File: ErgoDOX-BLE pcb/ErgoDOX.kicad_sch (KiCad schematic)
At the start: 102 parts, among them J1 Conn_01x04, J2 Conn_01x02_Female, J3 Conn_01x02_Female, J4 Conn_01x02, J5 Conn_01x02, J6 6PIN, P1 USB_C_Plug_USB2.0, Q1 Q_NPN_BCE, SW0:10 SW0:3, SW0:11 SW0:2, SW0:12 SW0:1, SW0:7 SW0:6, SW0:8 SW0:5, SW0:9 SW0:4, SW1:10 SW1:3, SW1:11 SW1:2, SW1:12 SW1:1, SW1:13 SW1:0, SW1:9 SW1:4, SW2:10 SW2:3, SW2:11 SW2:2, SW2:12 SW2:1, SW2:13 SW2:0, SW2:7 SW2:6, SW2:8 SW2:5, SW2:9 SW2:4, SW3:10 SW3:3, SW3:11 SW3:2, SW3:12 SW3:1, SW3:13 SW3:0, SW3:8 SW3:5, SW3:9 SW3:4, SW4:10 SW4:3, SW4:11 SW4:2, SW4:12 SW4:1, SW4:13 SW4:0, SW4:7 SW4:6, SW4:8 SW4:5, SW4:9 SW4:4, SW5:10 SW5:3, SW5:11 SW5:2, SW5:12 SW5:1, SW5:13 SW5:0, SW5:7 SW5:6, SW5:8 SW5:5, SW5:9 SW5:4, U1 MCP23018, U2 MCP23017_SP

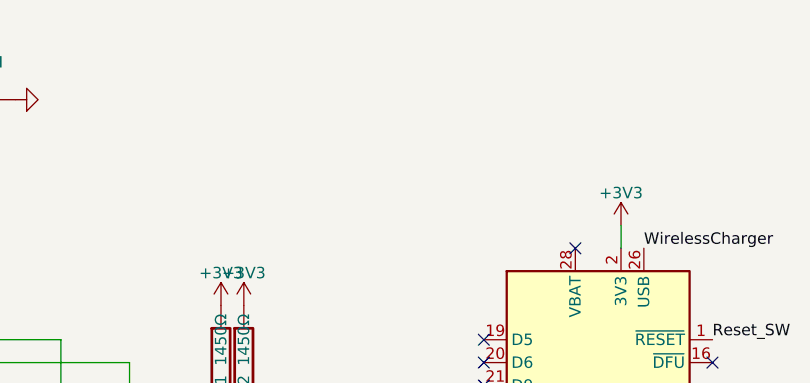
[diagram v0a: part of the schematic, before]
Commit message: Begin playing around with replacing the 23018 with a 23017
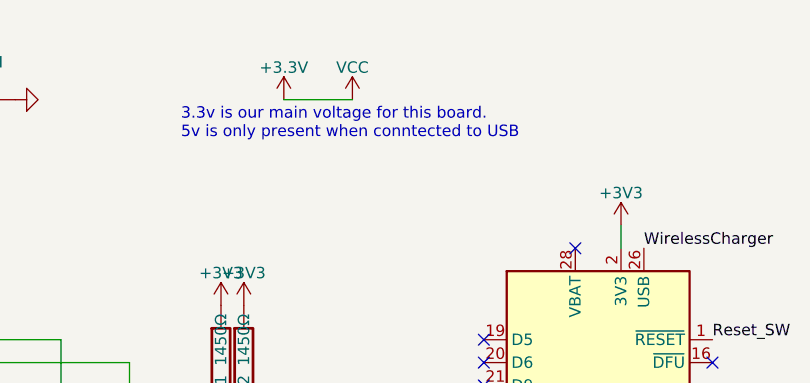
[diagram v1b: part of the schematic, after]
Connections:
- net VCC renamed +3.3V
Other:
- note added: "3.3v is our main voltage for this board. 5v is only present when conntected to USB"
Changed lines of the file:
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@@
     (stroke (width 0) (type default) (color 0 0 0 0))
   )
+  (wire (pts (xy 111.125 21.59) (xy 118.745 21.59))
+    (stroke (width 0) (type default) (color 0 0 0 0))
+  )
   (wire (pts (xy 58.42 196.85) (xy 76.2 196.85))
     (stroke (width 0) (type default) (color 0 0 0 0))
@@
     (effects (font (size 1.27 1.27)) (justify left bottom))
   )
+  (text "3.3v is our main voltage for this board.\n5v is only present when conntected to USB"
+    (at 99.695 26.035 0)
+    (effects (font (size 1.27 1.27)) (justify left bottom))
+  )
   (text "Backside footprint for MCU" (at 153.035 101.6 0)
     (effects (font (size 1.27 1.27)) (justify left bottom))
@@
     (pin "2")
   )
+  (symbol (lib_id "power:+3.3V") (at 111.125 21.59 0) (unit 1)
+    (in_bom yes) (on_board yes) (fields_autoplaced)
+    (property "Reference" "#PWR?" (id 0) (at 111.125 25.4 0)
+      (effects (font (size 1.27 1.27)) hide)
+    )
+    (property "Value" "+3.3V" (id 1) (at 111.125 18.0142 0))
+    (property "Footprint" "" (id 2) (at 111.125 21.59 0)
+      (effects (font (size 1.27 1.27)) hide)
+    )
+    (property "Datasheet" "" (id 3) (at 111.125 21.59 0)
+      (effects (font (size 1.27 1.27)) hide)
+    )
+    (pin "1")
+  )
+  (symbol (lib_id "power:VCC") (at 118.745 21.59 0) (unit 1)
+    (in_bom yes) (on_board yes) (fields_autoplaced)
+    (property "Reference" "#PWR?" (id 0) (at 118.745 25.4 0)
+      (effects (font (size 1.27 1.27)) hide)
+    )
+    (property "Value" "VCC" (id 1) (at 118.745 18.0142 0))
+    (property "Footprint" "" (id 2) (at 118.745 21.59 0)
+      (effects (font (size 1.27 1.27)) hide)
+    )
+    (property "Datasheet" "" (id 3) (at 118.745 21.59 0)
+      (effects (font (size 1.27 1.27)) hide)
+    )
+    (pin "1")
+  )
   (symbol (lib_id "Device:RotaryEncoder_Switch") (at 295.91 140.97 0) (unit 1)
     (in_bom yes) (on_board yes) (fields_autoplaced)
@@
       (reference "#PWR0107") (unit 1) (value "+5V") (footprint "")
     )
+    (path "/a649175b-f354-4397-a3b3-c0bd849b7072"
+      (reference "#PWR?") (unit 1) (value "+3.3V") (footprint "")
+    )
+    (path "/a9287306-e15a-4803-9f71-a2b7ca520be7"
+      (reference "#PWR?") (unit 1) (value "VCC") (footprint "")
+    )
     (path "/dc3e5149-0691-4e48-82aa-18a33c58d220"

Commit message: A lot of footprint work
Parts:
- removed U2: MCP23017_SP, Package_DIP:DIP-28_W7.62mm, symbol Interface_Expansion:MCP23017_SP
- C1: footprint Capacitor_THT:C_Axial_L5.1mm_D3.1mm_P7.50mm_Horizontal -> Capacitor_THT:CP_Radial_Tantal_D5.0mm_P5.00mm
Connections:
- net +3.3V is gone; now on net +3V3: U1.11 (VCC)
- no-connect marks 40 -> 38
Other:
- note added: "TODO: Need to double check the connector on size on this"
- note removed: "3.3v is our main voltage for this board. 5v is only present when conntected to USB"

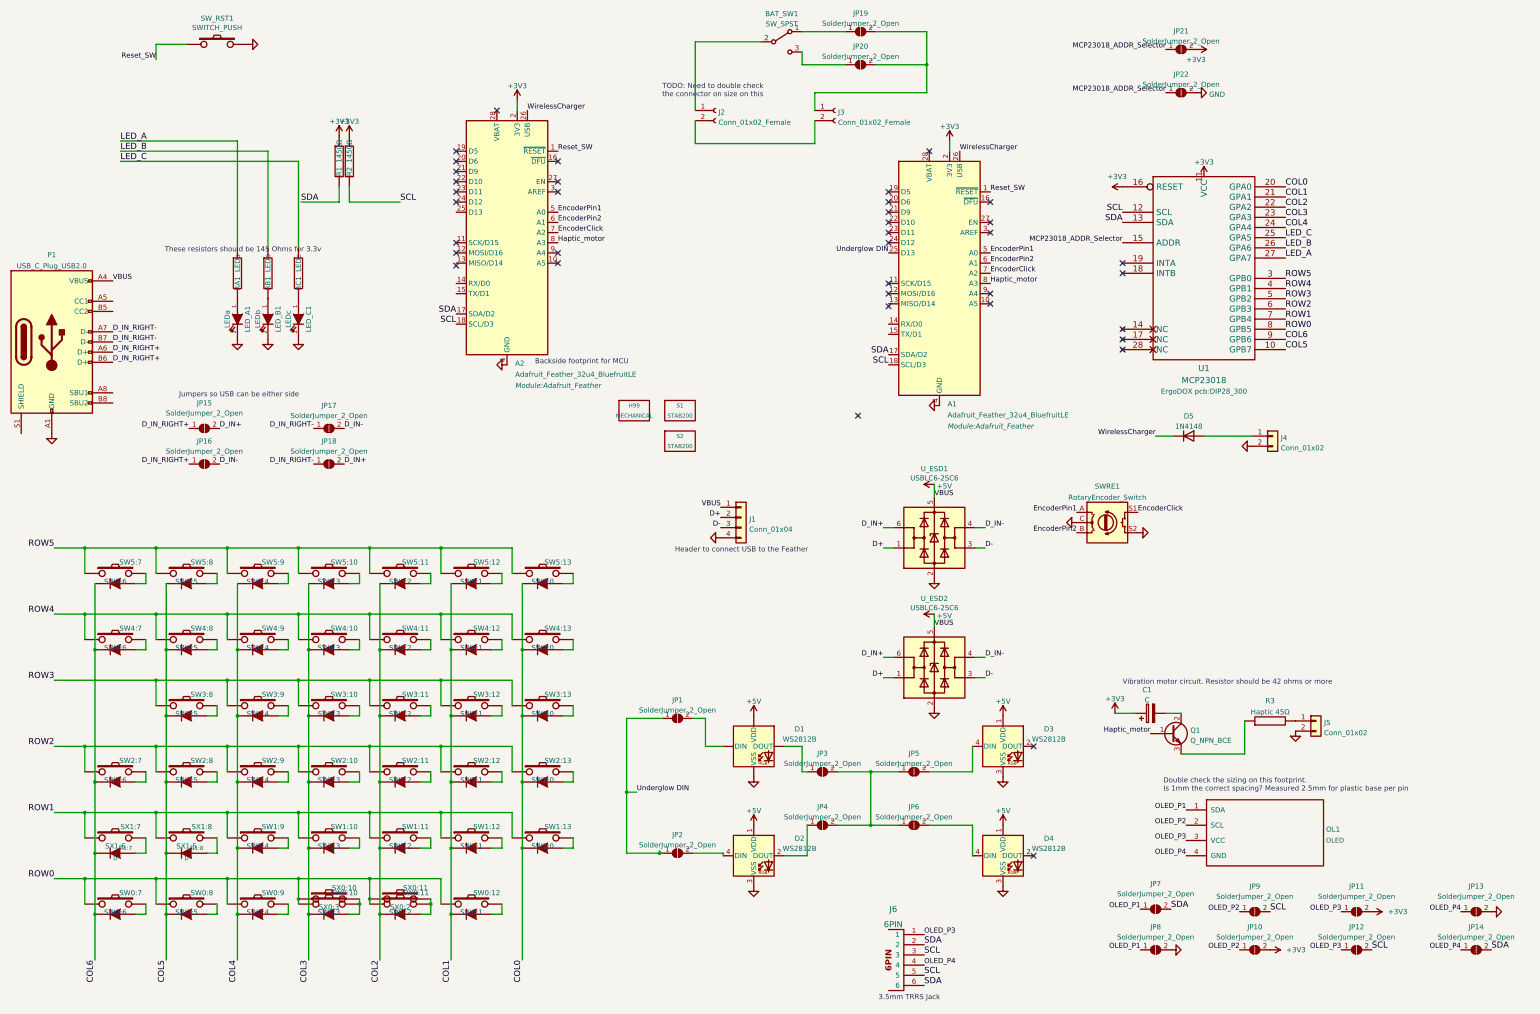
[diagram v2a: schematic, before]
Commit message: Adding a bunch of part numbers and verifying sizing
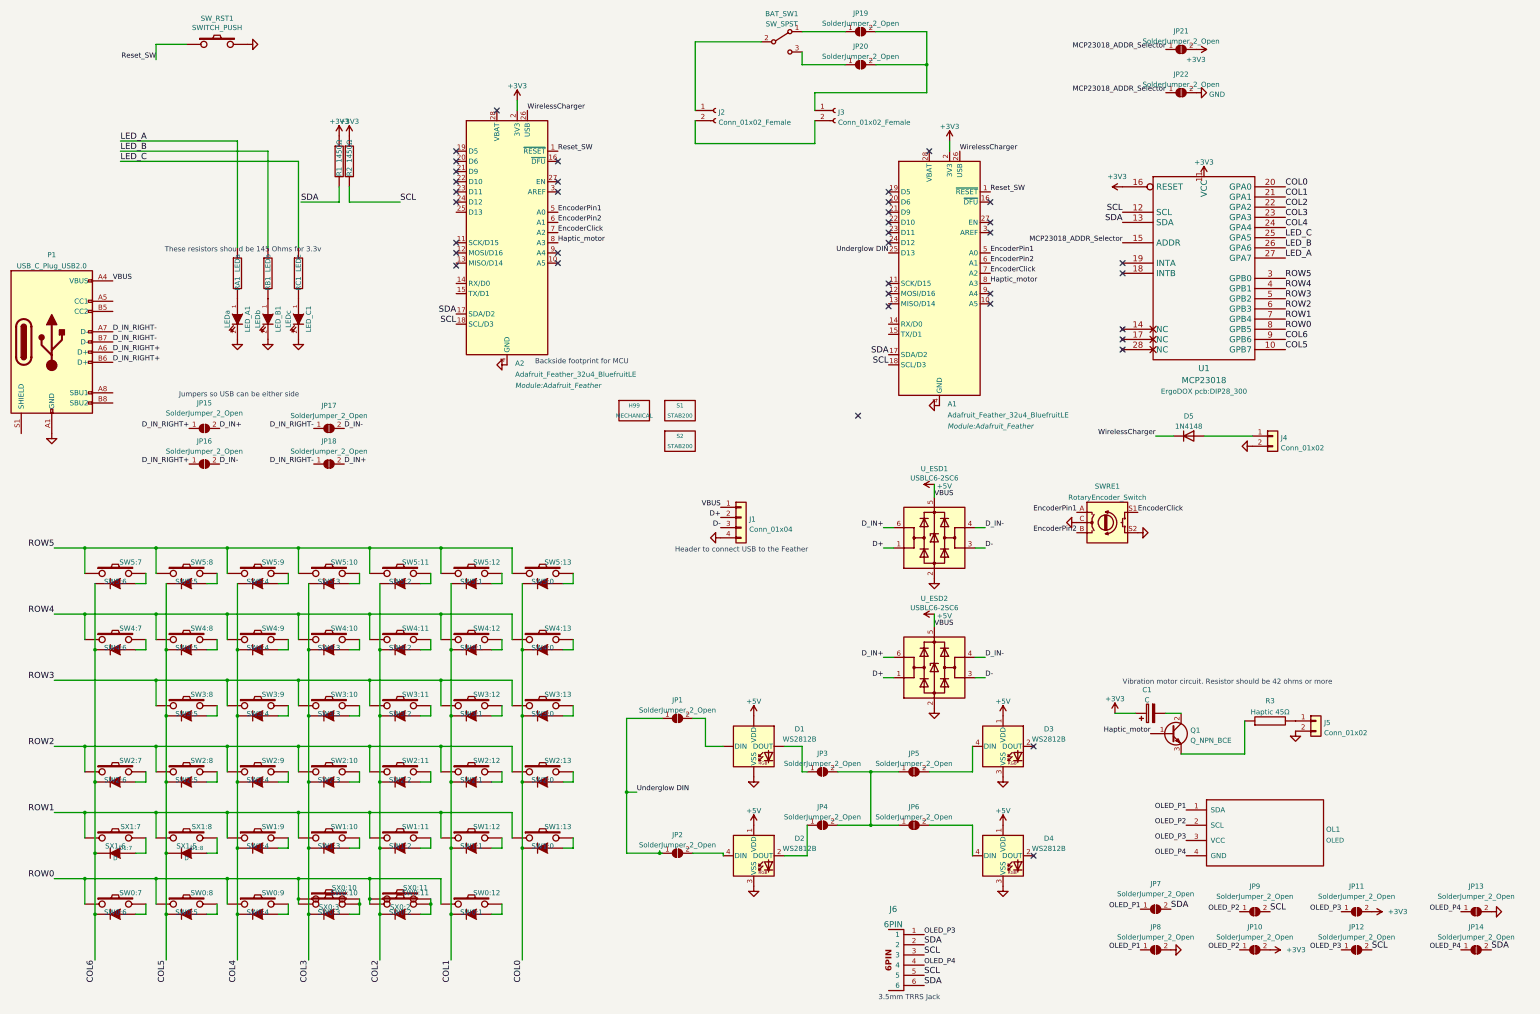
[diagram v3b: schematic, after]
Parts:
- BAT_SW1: manf# (none) -> EG1247
- J2, J3: manf# (none) -> B2B-PH-K-S(LF)(SN)
- J5: manf# (none) -> 316040001
- J6: manf# (none) -> SJ-43514
- P1: manf# (none) -> USB4085-GF-A
- U1: manf# (none) -> MCP23018-E/SP
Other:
- note removed: "Double check the sizing on this footprint. Is 1mm the correct spacing? Measured 2.5mm for plastic base per pin"
- note removed: "TODO: Need to double check the connector on size on this"
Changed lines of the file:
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@@
     (stroke (width 0) (type default) (color 0 0 0 0))
-  )
-  (text "TODO: Need to double check \nthe connector on size on this"
-    (at 184.785 34.925 0)
-    (effects (font (size 1.27 1.27)) (justify left bottom))
   )
   (text "These resistors should be 145 Ohms for 3.3v" (at 99.695 73.66 180)
@@
   )
   (text "Backside footprint for MCU" (at 153.035 101.6 0)
-    (effects (font (size 1.27 1.27)) (justify left bottom))
-  )
-  (text "Double check the sizing on this footprint.\nIs 1mm the correct spacing? Measured 2.5mm for plastic base per pin"
-    (at 309.88 208.28 0)
     (effects (font (size 1.27 1.27)) (justify left bottom))
   )
@@
     )
     (property "Datasheet" "https://www.usb.org/sites/default/files/documents/usb_type-c.zip" (id 3) (at 36.195 95.885 0)
+      (effects (font (size 1.27 1.27)) hide)
+    )
+    (property "manf#" "USB4085-GF-A" (id 4) (at 32.385 95.885 0)
       (effects (font (size 1.27 1.27)) hide)
     )
@@
       (effects (font (size 1.27 1.27)) hide)
     )
+    (property "manf#" "B2B-PH-K-S(LF)(SN)" (id 4) (at 227.965 38.1 0)
+      (effects (font (size 1.27 1.27)) hide)
+    )
     (pin "1")
     (pin "2")
@@
       (effects (font (size 1.27 1.27)) hide)
     )
+    (property "manf#" "SJ-43514" (id 4) (at 245.11 250.19 0)
+      (effects (font (size 1.27 1.27)) hide)
+    )
     (pin "1")
     (pin "2")
@@
     )
     (property "Datasheet" "~" (id 3) (at 347.98 190.5 0)
+      (effects (font (size 1.27 1.27)) hide)
+    )
+    (property "manf#" "316040001" (id 4) (at 347.98 190.5 0)
       (effects (font (size 1.27 1.27)) hide)
     )
@@
     (property "Footprint" "ErgoDOX pcb:DIP28_300" (id 2) (at 320.04 108.2202 0))
     (property "Datasheet" "" (id 3) (at 320.04 77.47 0)
+      (effects (font (size 1.27 1.27)) hide)
+    )
+    (property "manf#" "MCP23018-E/SP" (id 4) (at 320.04 77.47 0)
       (effects (font (size 1.27 1.27)) hide)
     )
@@
       (effects (font (size 1.27 1.27)) hide)
     )
+    (property "manf#" "B2B-PH-K-S(LF)(SN)" (id 4) (at 198.12 38.1 0)
+      (effects (font (size 1.27 1.27)) hide)
+    )
     (pin "1")
     (pin "2")
@@
       (effects (font (size 1.27 1.27)) hide)
     )
+    (property "manf#" "EG1247" (id 4) (at 214.63 20.955 0)
+      (effects (font (size 1.27 1.27)) hide)
+    )

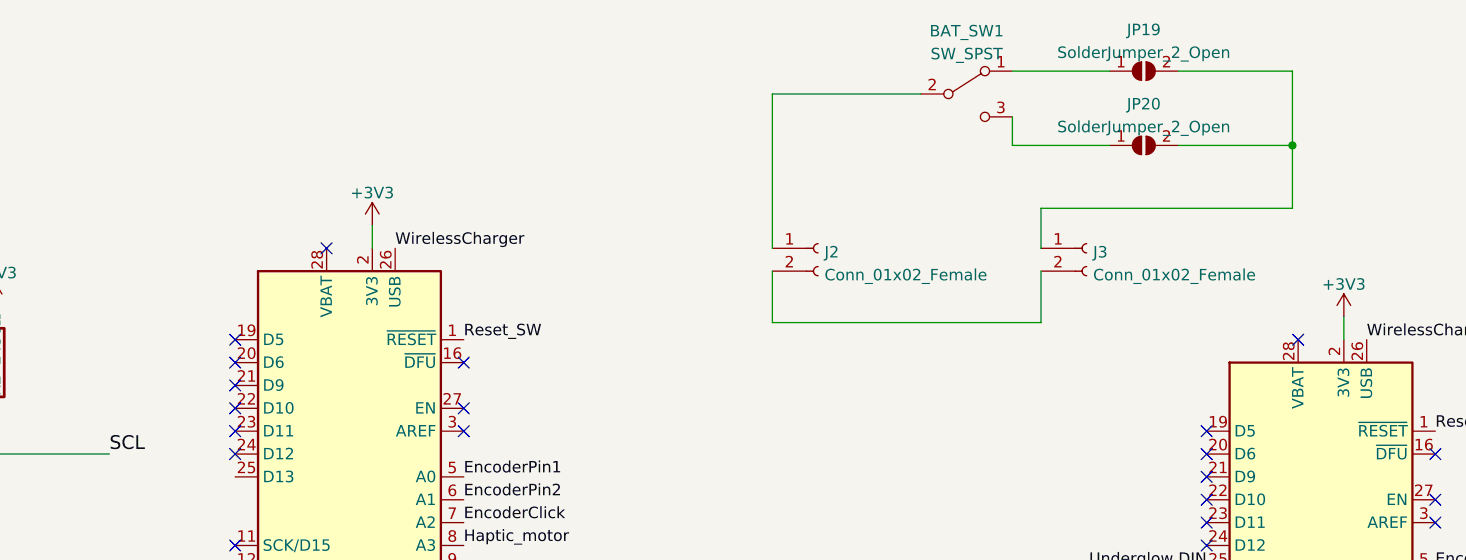
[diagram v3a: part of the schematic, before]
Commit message: Remove PCB to MCU JST connector, add mech hole for battery cable
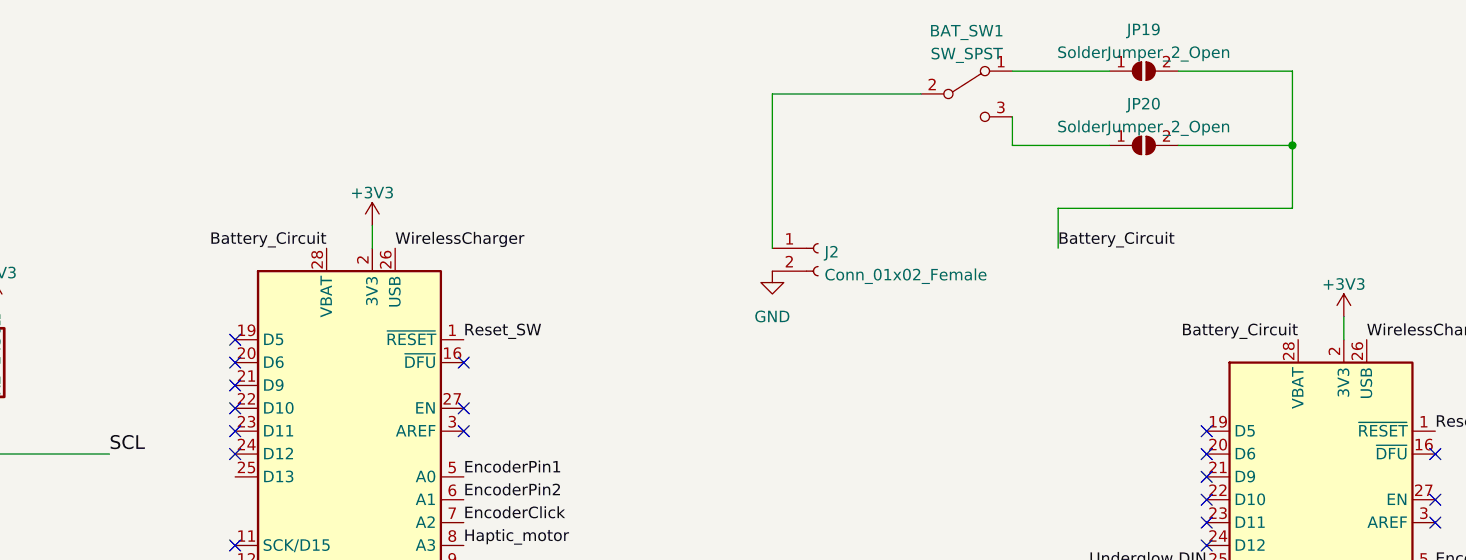
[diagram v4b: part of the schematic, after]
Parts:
- removed J3: Conn_01x02_Female, Connector_JST:JST_EH_B2B-EH-A_1x02_P2.50mm_Vertical, symbol Connector:Conn_01x02_Female
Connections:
- net GND: now also J2.2 (Pin_2)
- net Battery_Circuit: now reaches JP19.2 (B), JP20.2 (B)
- net Battery_Circuit: now also A1.28 (VBAT), A2.28 (VBAT)
- no-connect marks 38 -> 36
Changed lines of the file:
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@@
   (no_connect (at 266.7 66.04))
   (no_connect (at 266.7 68.58))
-  (no_connect (at 143.51 38.1))
   (no_connect (at 241.3 81.28))
   (no_connect (at 241.3 83.82))
@@
   (no_connect (at 158.75 50.8))
   (no_connect (at 133.35 53.34))
-  (no_connect (at 251.46 48.26))
   (no_connect (at 233.68 114.3))
   (no_connect (at 158.75 73.66))
@@
     (stroke (width 0) (type default) (color 0 0 0 0))
   )
-  (wire (pts (xy 222.885 46.355) (xy 222.885 40.64))
-    (stroke (width 0) (type default) (color 0 0 0 0))
-  )
   (wire (pts (xy 127 234.95) (xy 127 236.22))
     (stroke (width 0) (type default) (color 0 0 0 0))
@@
     (stroke (width 0) (type default) (color 0 0 0 0))
   )
-  (wire (pts (xy 193.04 46.355) (xy 222.885 46.355))
-    (stroke (width 0) (type default) (color 0 0 0 0))
-  )
   (wire (pts (xy 124.46 222.25) (xy 127 222.25))
     (stroke (width 0) (type default) (color 0 0 0 0))
@@
     (stroke (width 0) (type default) (color 0 0 0 0))
   )
-  (wire (pts (xy 193.04 40.64) (xy 193.04 46.355))
-    (stroke (width 0) (type default) (color 0 0 0 0))
-  )
   (wire (pts (xy 91.44 205.74) (xy 91.44 203.2))
     (stroke (width 0) (type default) (color 0 0 0 0))
@@
     (stroke (width 0) (type default) (color 0 0 0 0))
   )
-  (wire (pts (xy 250.825 33.655) (xy 222.885 33.655))
+  (wire (pts (xy 250.825 33.655) (xy 224.79 33.655))
     (stroke (width 0) (type default) (color 0 0 0 0))
   )
@@
     (stroke (width 0) (type default) (color 0 0 0 0))
   )
-  (wire (pts (xy 222.885 33.655) (xy 222.885 38.1))
+  (wire (pts (xy 224.79 33.655) (xy 224.79 38.1))
     (stroke (width 0) (type default) (color 0 0 0 0))
   )
@@
     (effects (font (size 1.27 1.27)) (justify right bottom))
   )
+  (label "Battery_Circuit" (at 224.79 38.1 0)
+    (effects (font (size 1.27 1.27)) (justify left bottom))
+  )
   (label "D_IN_RIGHT-" (at 97.79 126.365 180)
     (effects (font (size 1.27 1.27)) (justify right bottom))
@@
     (effects (font (size 1.27 1.27)) (justify left bottom))
   )
+  (label "Battery_Circuit" (at 143.51 38.1 180)
+    (effects (font (size 1.27 1.27)) (justify right bottom))
+  )
   (label "D-" (at 265.43 179.705 0)
     (effects (font (size 1.27 1.27)) (justify left bottom))
@@
     (effects (font (size 1.524 1.524)) (justify left bottom))
   )
+  (label "Battery_Circuit" (at 251.46 48.26 180)
+    (effects (font (size 1.27 1.27)) (justify right bottom))
+  )
   (label "SCL" (at 336.55 238.125 0)
     (effects (font (size 1.524 1.524)) (justify left bottom))
@@
     (pin "1")
   )
-  (symbol (lib_id "Connector:Conn_01x02_Female") (at 227.965 38.1 0) (unit 1)
-    (in_bom yes) (on_board yes) (fields_autoplaced)
-    (property "Reference" "J3" (id 0) (at 228.6762 38.5353 0)
-      (effects (font (size 1.27 1.27)) (justify left))
-    )
-    (property "Value" "Conn_01x02_Female" (id 1) (at 228.6762 41.0722 0)
-      (effects (font (size 1.27 1.27)) (justify left))
-    )
-    (property "Footprint" "Connector_JST:JST_EH_B2B-EH-A_1x02_P2.50mm_Vertical" (id 2) (at 227.965 38.1 0)
-      (effects (font (size 1.27 1.27)) hide)
-    )
-    (property "Datasheet" "~" (id 3) (at 227.965 38.1 0)
-      (effects (font (size 1.27 1.27)) hide)
-    )
-    (property "manf#" "B2B-PH-K-S(LF)(SN)" (id 4) (at 227.965 38.1 0)
-      (effects (font (size 1.27 1.27)) hide)
-    )
-    (pin "1")
-    (pin "2")
-  )
   (symbol (lib_id "Jumper:SolderJumper_2_Open") (at 224.79 216.535 0) (unit 1)
     (in_bom yes) (on_board yes) (fields_autoplaced)
@@
     (pin "1")
   )
+  (symbol (lib_name "GND_1") (lib_id "power:GND") (at 193.04 40.64 0) (unit 1)
+    (in_bom yes) (on_board yes) (fields_autoplaced)
+    (property "Reference" "#PWR?" (id 0) (at 193.04 46.99 0)
+      (effects (font (size 1.27 1.27)) hide)
+    )
+    (property "Value" "GND" (id 1) (at 193.04 45.72 0))
+    (property "Footprint" "" (id 2) (at 193.04 40.64 0)
+      (effects (font (size 1.27 1.27)) hide)
+    )
+    (property "Datasheet" "" (id 3) (at 193.04 40.64 0)
+      (effects (font (size 1.27 1.27)) hide)
+    )
+    (pin "1")
+  )
   (symbol (lib_id "component:GND") (at 287.02 140.97 270) (unit 1)
     (in_bom yes) (on_board yes) (fields_autoplaced)
@@
       (reference "#PWR0107") (unit 1) (value "+5V") (footprint "")
     )
+    (path "/7dfa7247-12a0-4888-9d03-1bdfdd878cd3"
+      (reference "#PWR?") (unit 1) (value "GND") (footprint "")
+    )
     (path "/dc3e5149-0691-4e48-82aa-18a33c58d220"
       (reference "A1") (unit 1) (value "Adafruit_Feather_32u4_BluefruitLE") (footprint "Module:Adafruit_Feather")
@@
       (reference "J2") (unit 1) (value "Conn_01x02_Female") (footprint "Connector_JST:JST_EH_B2B-EH-A_1x02_P2.50mm_Vertical")
     )
-    (path "/261c313c-6bc0-4689-9896-45bdc65d1b10"
-      (reference "J3") (unit 1) (value "Conn_01x02_Female") (footprint "Connector_JST:JST_EH_B2B-EH-A_1x02_P2.50mm_Vertical")
-    )
     (path "/5904efe1-74e9-4f91-bd0f-5ccb604231d8"
